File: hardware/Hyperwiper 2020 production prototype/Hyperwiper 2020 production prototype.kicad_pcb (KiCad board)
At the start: 2 copper layers, 79.5 x 57.3 mm, 19 parts, among them K1 Main Power relay, K2 Wiper control relay, Q1 PN2222A, U1 Teensy4.0, U3 L7805, X1 W237-3E-bGeigieNanoKit_V1.1r5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, X2 W237-3E-bGeigieNanoKit_V1.1r5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

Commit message: updated kicad files with new traced board
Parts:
- moved Q1 12.6 mm to (934.1, 40.8)
- moved D2 3.05 mm to (942.8, 54.5)
- moved D1 2.04 mm to (951.7, 54.5)
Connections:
- K1 pad 2: (no net) -> Net-(K1-Pad2)
- K2 pad 4: (no net) -> Net-(K2-Pad4)
- R1 pad 1: (no net) -> /motor_start
- R4 pad 1: (no net) -> /M_LED_b
- R5 pad 1: (no net) -> /M_LED_g
- R6 pad 1: (no net) -> /M_LED_r
- R7 pad 1: (no net) -> /B_LED_b
- R8 pad 1: (no net) -> /B_LED_g
- R9 pad 1: (no net) -> /B_LED_r
- RV1 pad 2: (no net) -> /Pot
- U1 pad 1: (no net) -> Net-(U1-Pad1)
- U1 pad 10: (no net) -> Net-(U1-Pad10)
- U1 pad 11: (no net) -> Net-(U1-Pad11)
- U1 pad 12: (no net) -> Net-(U1-Pad12)
- U1 pad 13: (no net) -> Net-(U1-Pad13)
- U1 pad 14: (no net) -> Net-(U1-Pad14)
- U1 pad 15: (no net) -> Net-(U1-Pad15)
- U1 pad 16: (no net) -> Net-(U1-Pad16)
- U1 pad 17: (no net) -> Net-(U1-Pad17)
- U1 pad 18: (no net) -> Net-(U1-Pad18)
- U1 pad 19: (no net) -> Net-(U1-Pad19)
- U1 pad 2: (no net) -> Net-(U1-Pad2)
- U1 pad 20: (no net) -> Net-(U1-Pad20)
- U1 pad 21: (no net) -> Net-(U1-Pad21)
- U1 pad 22: (no net) -> Net-(U1-Pad22)
- U1 pad 23: (no net) -> Net-(U1-Pad23)
- U1 pad 24: (no net) -> Net-(U1-Pad24)
- U1 pad 25: (no net) -> Net-(U1-Pad25)
- U1 pad 26: (no net) -> Net-(U1-Pad26)
- U1 pad 27: (no net) -> Net-(U1-Pad27)
- U1 pad 28: (no net) -> Net-(U1-Pad28)
- U1 pad 29: (no net) -> Net-(U1-Pad29)
- U1 pad 3: (no net) -> Net-(U1-Pad3)
- U1 pad 30: (no net) -> Net-(U1-Pad30)
- U1 pad 31: (no net) -> Net-(U1-Pad31)
- U1 pad 34: (no net) -> Net-(U1-Pad34)
- U1 pad 35: (no net) -> Net-(U1-Pad35)
- U1 pad 36: (no net) -> Net-(U1-Pad36)
- U1 pad 37: (no net) -> Net-(U1-Pad37)
- U1 pad 38: (no net) -> Net-(U1-Pad38)
- U1 pad 39: (no net) -> Net-(U1-Pad39)
- U1 pad 4: (no net) -> Net-(U1-Pad4)
- U1 pad 40: (no net) -> Net-(U1-Pad40)
- U1 pad 41: (no net) -> Net-(U1-Pad41)
- U1 pad 42: (no net) -> Net-(U1-Pad42)
- U1 pad 43: (no net) -> Net-(U1-Pad43)
- U1 pad 44: (no net) -> Net-(U1-Pad44)
- U1 pad 5: (no net) -> Net-(U1-Pad5)
- U1 pad 6: (no net) -> Net-(U1-Pad6)
- U1 pad 7: (no net) -> Net-(U1-Pad7)
- U1 pad 8: (no net) -> Net-(U1-Pad8)
- U1 pad 9: (no net) -> Net-(U1-Pad9)
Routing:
- net GND: track 130.3 -> 167.9 mm
- net Net-(D1-Pad4): track 34.8 -> 60.4 mm
- net Net-(K2-Pad2): track 45.6 -> 31.3 mm
- net Net-(D1-Pad2): track 23.6 -> 30.5 mm, vias 0 -> 1
- net Net-(D1-Pad3): track 37.4 -> 43.2 mm, vias 0 -> 1
- net Net-(D2-Pad2): track 52.2 -> 56.9 mm
- net /5V: track 114.4 -> 110.1 mm
- net Net-(D2-Pad4): track 31.5 -> 34.6 mm
- net Net-(D2-Pad3): track 35.3 -> 38.3 mm
- net Net-(Q1-Pad2): track 57.7 -> 59.9 mm
- net Net-(K1-Pad4): track 51.7 -> 53.5 mm

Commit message: Updated board
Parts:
- added SW1: ON-OFF, Button_Switch_THT:SW_Tactile_SPST_Angled_PTS645Vx83-2LFS, F.Cu at (902.7, 33.7)
- moved Q1 29.4 mm to (905.1, 45.6)
- moved U3 18.6 mm to (904.6, 17.5)
- moved X1 2.44 mm to (912.7, 56.3)
- moved X2 2.44 mm to (929.1, 56.3)
- moved D2 0.65 mm to (943.5, 54.4)
- moved D1 0.13 mm to (951.7, 54.4)
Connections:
- D1 pad 1: GND -> Net-(D1-Pad1)
- D1 pad 2: Net-(D1-Pad2) -> GND
- D2 pad 1: GND -> Net-(D2-Pad1)
- D2 pad 2: Net-(D2-Pad2) -> GND
- R4 pad 2: Net-(D1-Pad4) -> Net-(D1-Pad3)
- R5 pad 2: Net-(D1-Pad3) -> Net-(D1-Pad4)
- R6 pad 2: Net-(D1-Pad2) -> Net-(D1-Pad1)
- R7 pad 2: Net-(D2-Pad4) -> Net-(D2-Pad3)
- R8 pad 2: Net-(D2-Pad3) -> Net-(D2-Pad4)
- R9 pad 2: Net-(D2-Pad2) -> Net-(D2-Pad1)
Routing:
- net Net-(D2-Pad1): track 0.00 -> 72.0 mm
- net Net-(D2-Pad2): track 56.9 -> 0.00 mm
- net Net-(Q1-Pad2): track 59.9 -> 95.7 mm
- net Net-(D1-Pad2): track 30.5 -> 0.00 mm, vias 1 -> 0
- net Net-(D1-Pad1): track 0.00 -> 30.0 mm
- net Net-(K1-Pad4): track 53.5 -> 80.5 mm
- net Net-(K2-Pad2): track 31.3 -> 57.8 mm
- net Net-(K1-Pad2): track 0.00 -> 23.5 mm
- net GND: track 167.9 -> 181.6 mm
- net Net-(K1-Pad3): track 25.6 -> 30.7 mm
- net Net-(D2-Pad4): track 34.6 -> 37.5 mm
- net /5V: track 110.1 -> 107.7 mm
- net Net-(D1-Pad4): track 60.4 -> 62.1 mm
- net Net-(K1-Pad1): track 51.8 -> 53.1 mm
- net Net-(D2-Pad3): track 38.3 -> 37.3 mm
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
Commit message: Updated  schematic
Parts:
- moved D1 802.1 mm to (151.2, 103.6)
- moved D2 802.1 mm to (142.9, 103.6)
- moved D3 802.1 mm to (171.2, 102.3)
- moved K1 802.1 mm to (125.7, 85.4)
- moved K2 802.1 mm to (125.8, 66.9)
- moved Q1 802.1 mm to (104.6, 94.8)
- moved R1 802.1 mm to (164.6, 60.7)
- moved R3 802.1 mm to (174.8, 65.1)
- moved R4 802.1 mm to (165.5, 81.6)
- moved R5 802.1 mm to (169.7, 81.6)
- moved R6 802.1 mm to (165.5, 95.0)
- moved R7 802.1 mm to (169.7, 95.0)
- moved R8 802.1 mm to (173.8, 95.0)
- moved R9 802.1 mm to (173.8, 81.6)
- moved RV1 802.1 mm to (160.1, 105.4)
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
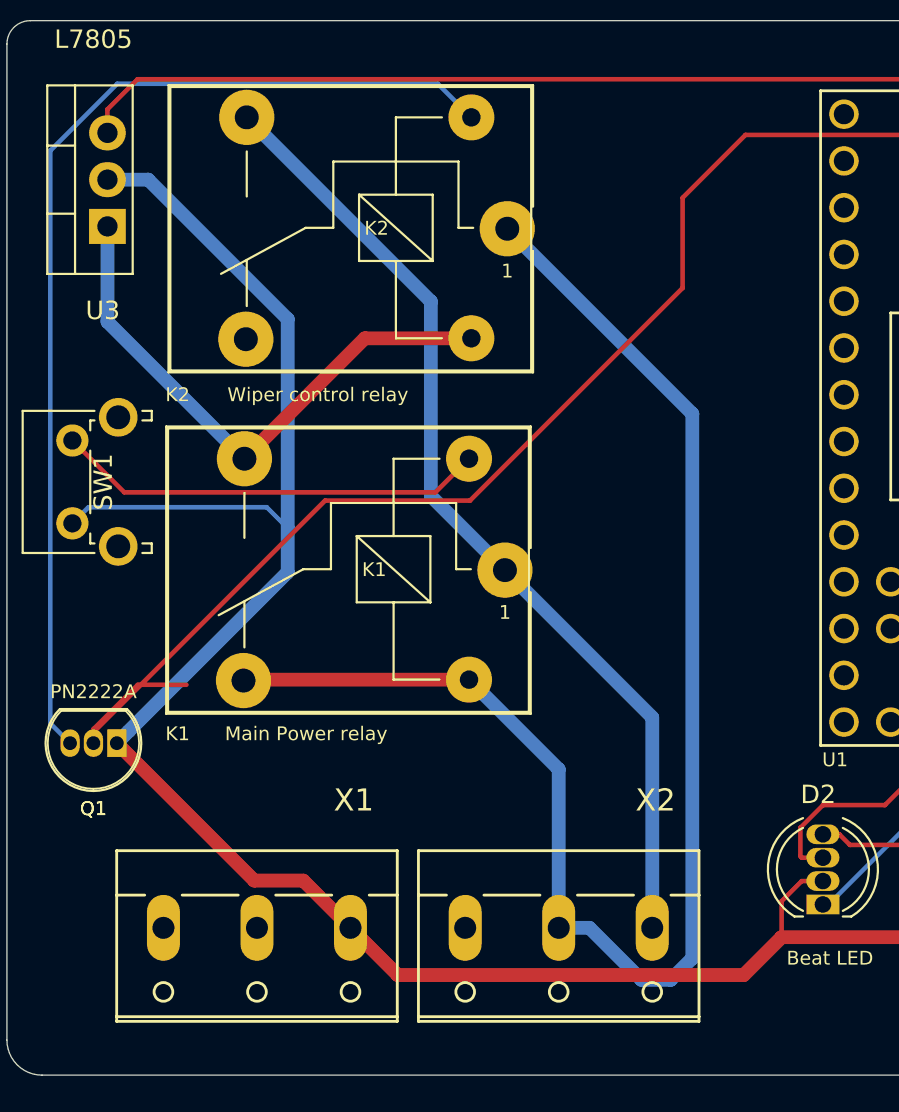
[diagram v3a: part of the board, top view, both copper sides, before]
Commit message: Changes schemtic. Mistake in wireing
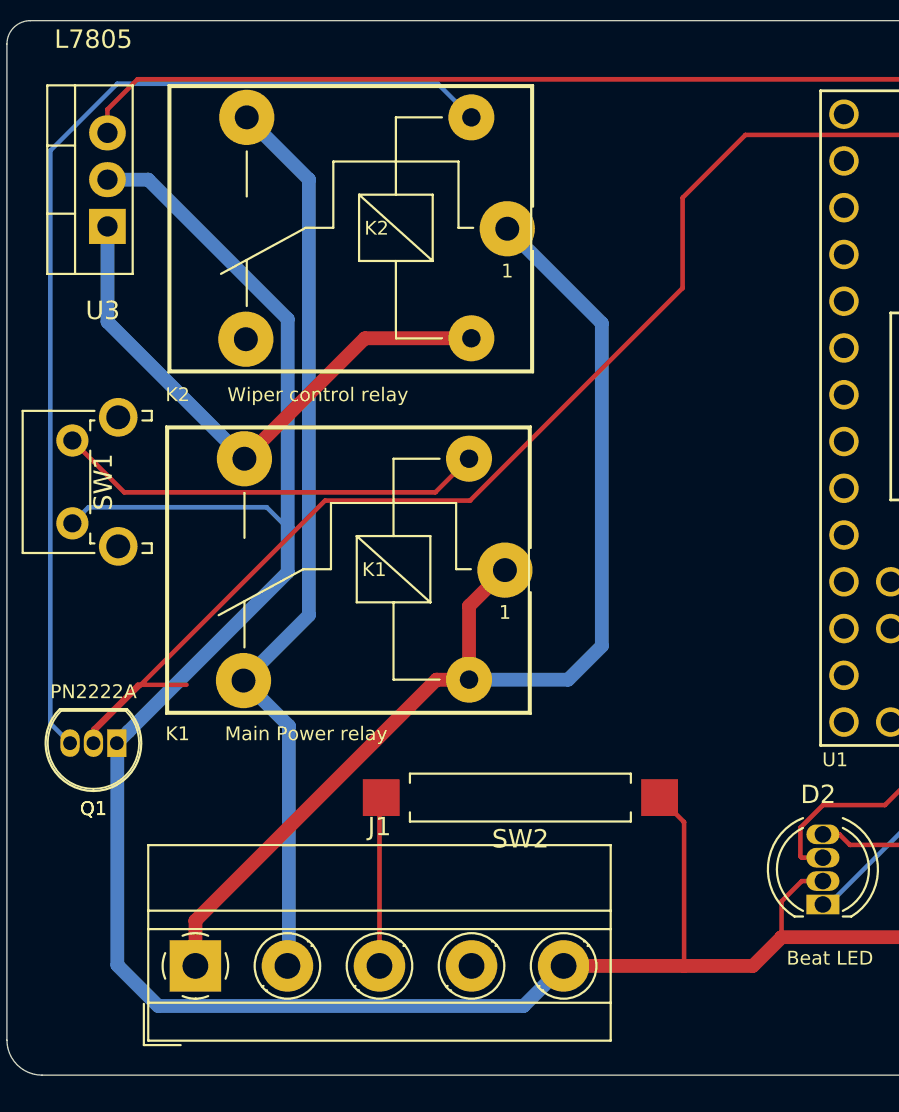
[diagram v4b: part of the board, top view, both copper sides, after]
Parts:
- removed X1, X2: W237-3E-bGeigieNanoKit_V1.1r5a-eagle-import, DWP 2020:W237-3E
- added J1: Conn_01x05, TerminalBlock_MetzConnect:TerminalBlock_MetzConnect_Type011_RT05505HBWC_1x05_P5.00mm_Horizontal, F.Cu at (108.8, 106.9)
- added SW2: SW_Reed, Button_Switch_SMD:SW_SPST_REED_CT10-XXXX-G1, F.Cu at (126.5, 97.8)
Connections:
- K1 pad 1: Net-(K1-Pad1) -> Net-(J1-Pad1)
- K1 pad 4: Net-(K1-Pad4) -> Net-(J1-Pad2)
- K1 pad 5: Net-(K1-Pad4) -> Net-(J1-Pad1)
- K2 pad 1: Net-(K1-Pad4) -> Net-(J1-Pad1)
- K2 pad 3: Net-(K1-Pad1) -> Net-(J1-Pad2)
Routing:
- net Net-(K1-Pad4): track 80.5 -> 0.00 mm
- net Net-(J1-Pad1): track 0.00 -> 65.2 mm
- net Net-(K1-Pad1): track 53.1 -> 0.00 mm
- net Net-(J1-Pad2): track 0.00 -> 50.1 mm
- net GND: track 181.6 -> 199.8 mm
- net /reed: track 0.00 -> 9.18 mm

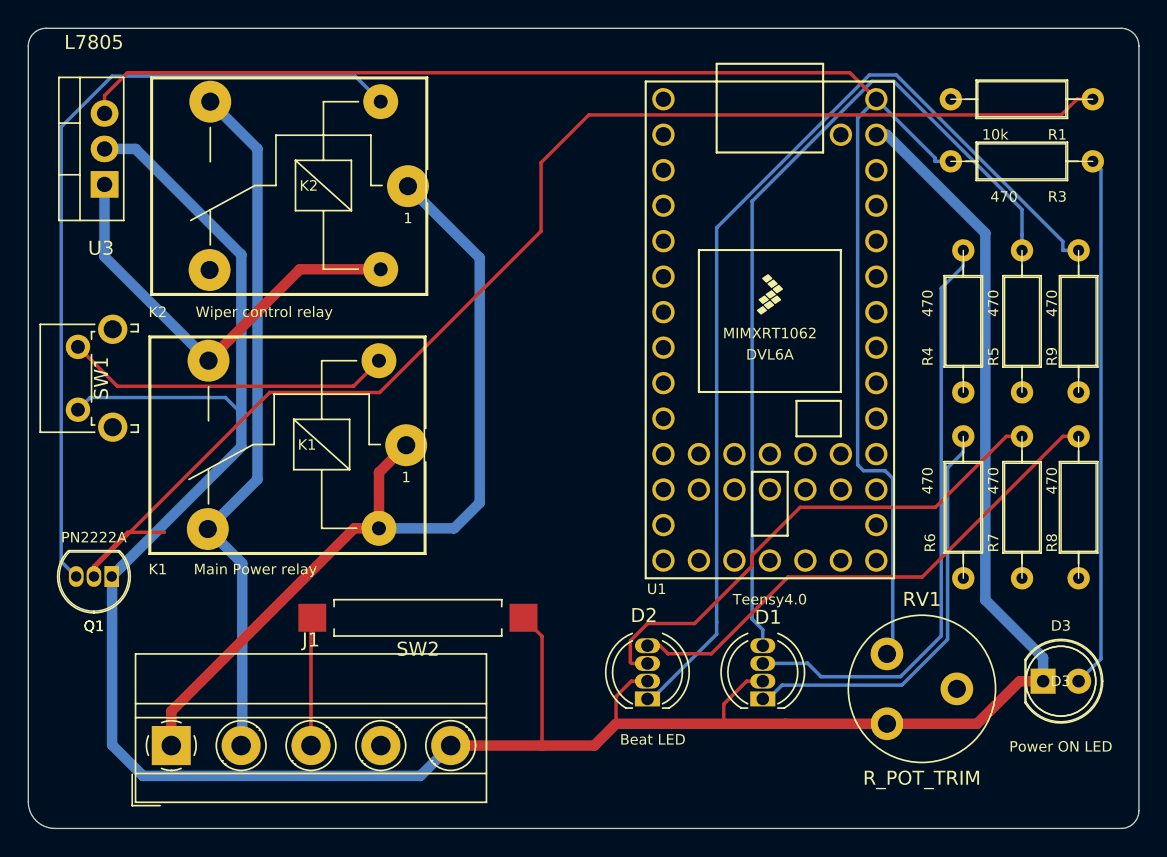
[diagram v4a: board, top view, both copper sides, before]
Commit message: Adde routing for the RGB leds
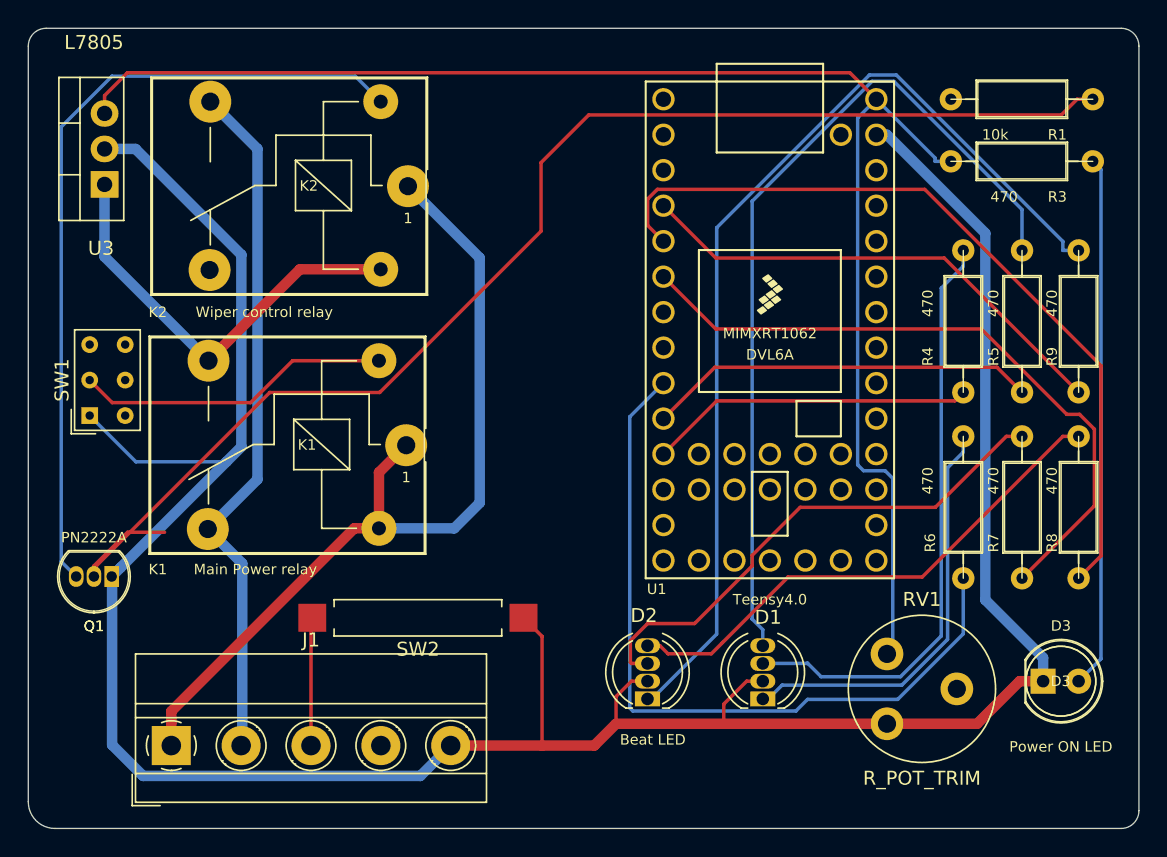
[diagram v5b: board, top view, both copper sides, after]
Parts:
- SW1: footprint Button_Switch_THT:SW_Tactile_SPST_Angled_PTS645Vx83-2LFS -> Button_Switch_THT:SW_NKK_GW12LJP
- moved SW1 0.94 mm to (103.0, 83.3)
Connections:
- U1 pad 10: Net-(U1-Pad10) -> /M_LED_g
- U1 pad 11: Net-(U1-Pad11) -> /M_LED_b
- U1 pad 4: Net-(U1-Pad4) -> /B_LED_r
- U1 pad 5: Net-(U1-Pad5) -> /B_LED_g
- U1 pad 6: Net-(U1-Pad6) -> /B_LED_b
- U1 pad 9: Net-(U1-Pad9) -> /M_LED_r
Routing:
- net /B_LED_g: track 0.00 -> 57.3 mm
- net /M_LED_r: track 0.00 -> 54.5 mm
- net /B_LED_b: track 0.00 -> 48.2 mm
- net /B_LED_r: track 0.00 -> 35.3 mm
- net /M_LED_g: track 0.00 -> 27.9 mm
- net /M_LED_b: track 0.00 -> 23.3 mm
- net GND: track 199.8 -> 198.6 mm
- net Net-(K1-Pad2): track 23.5 -> 22.6 mm

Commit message: Updated schematics
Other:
- board text added: "HyperWiperPrototype V0.9"
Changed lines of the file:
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@@
       (effects (font (size 0.75 0.75) (thickness 0.15)))
     )
-    (fp_text value "Teensy4.0" (at 19.304 0 unlocked) (layer "F.SilkS")
+    (fp_text value "Teensy4.0" (at 18.8325 -0.458 unlocked) (layer "F.SilkS")
       (effects (font (size 0.75 0.75) (thickness 0.15)))
     )
@@
   (gr_arc (start 99.872 56.8595) (end 99.872 55.5895) (angle -90) (layer "Edge.Cuts") (width 0.05))
   (gr_arc (start 176.834 111.5965) (end 176.834 112.8665) (angle -90) (layer "Edge.Cuts") (width 0.05))
+  (gr_text "HyperWiperPrototype   V0.9   \n" (at 117.856 98.552) (layer "B.SilkS")
+    (effects (font (size 1.5 1.5) (thickness 0.3)) (justify mirror))
+  )
+  (gr_text "HyperWiperPrototype   V0.9   \n" (at 134.112 76.073 90) (layer "F.SilkS")
+    (effects (font (size 1.5 1.5) (thickness 0.3)))
+  )
   (segment (start 104.063 60.4065) (end 105.697 58.7725) (width 0.25) (layer "F.Cu") (net 1))
   (segment (start 157.411 58.7725) (end 159.308 60.6695) (width 0.25) (layer "F.Cu") (net 1))
